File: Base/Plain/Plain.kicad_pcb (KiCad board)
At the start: 2 copper layers, 30 x 84 mm, 13 parts, among them J1 Barrel_Jack_Switch, J2 AudioJack2_Ground, J3 AudioJack2_Ground, J4 Conn_01x04_Pin, Q1 40V

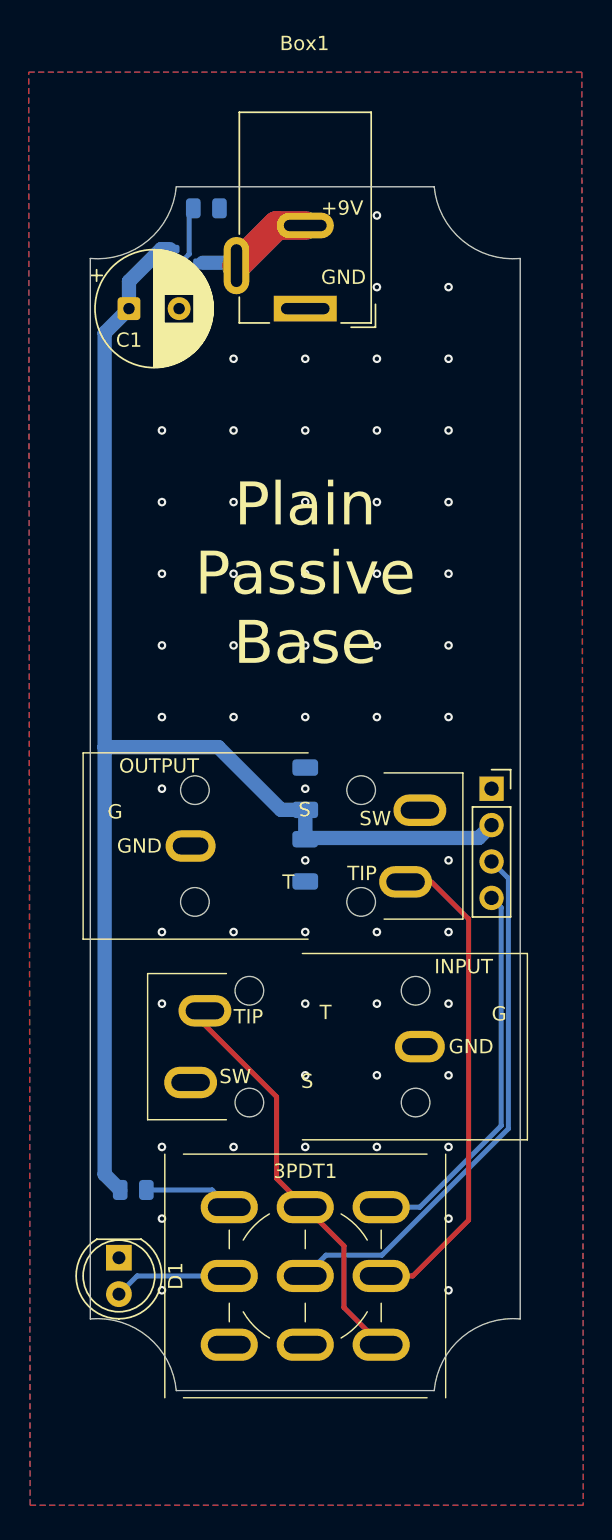
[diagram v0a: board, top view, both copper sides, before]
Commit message: First revisions from gen3 testing...
It turns out that while the single connector was sufficient, it is also
mechanically annoyingly less robust than the two separate pin headers we
used to have.

So even though we don't need the extra pins, just split it up into
"power" and a "signal" connectors again.  The placement behind the
output jack was good, so just put the power jack behind the input one
instead.

That ends up making routing nicer with the power trace going down where
it needs to be for the LED anyway, so it's a win-win.  Much nicer than
the old board.  And with the extra pins and the position right next to
the LED, lets just make the base board LED voltage available as an
"active" signal in case anybody ever wants it.

Also, just move the DC blocking capacitor and the anti-pop resistor to
ground to the base board.  Any effects board needs to do that, so it's
one less thing to worry about.  Also add back the low pass RF filter.

With the connector change, this obviously makes the new boards
incompatible, but it's not like I have any legacy boards except for the
test-boards.

On the effect board side, this does the layout changes, but also fixes
the Octaver board that was half-arsed and hadn't done proper bias
voltage calculations.  This basically just reuses them from the boost
board.

Plus use a JFET input on for the Octaver, and while at it make it also
just split the phase the natural way.  Both simpler and more balanced.

So maybe the Octaver works now.

And by "works", I obviously don't mean "sounds good".

Signed-off-by: Linus Torvalds <torvalds@linux-foundation.org>
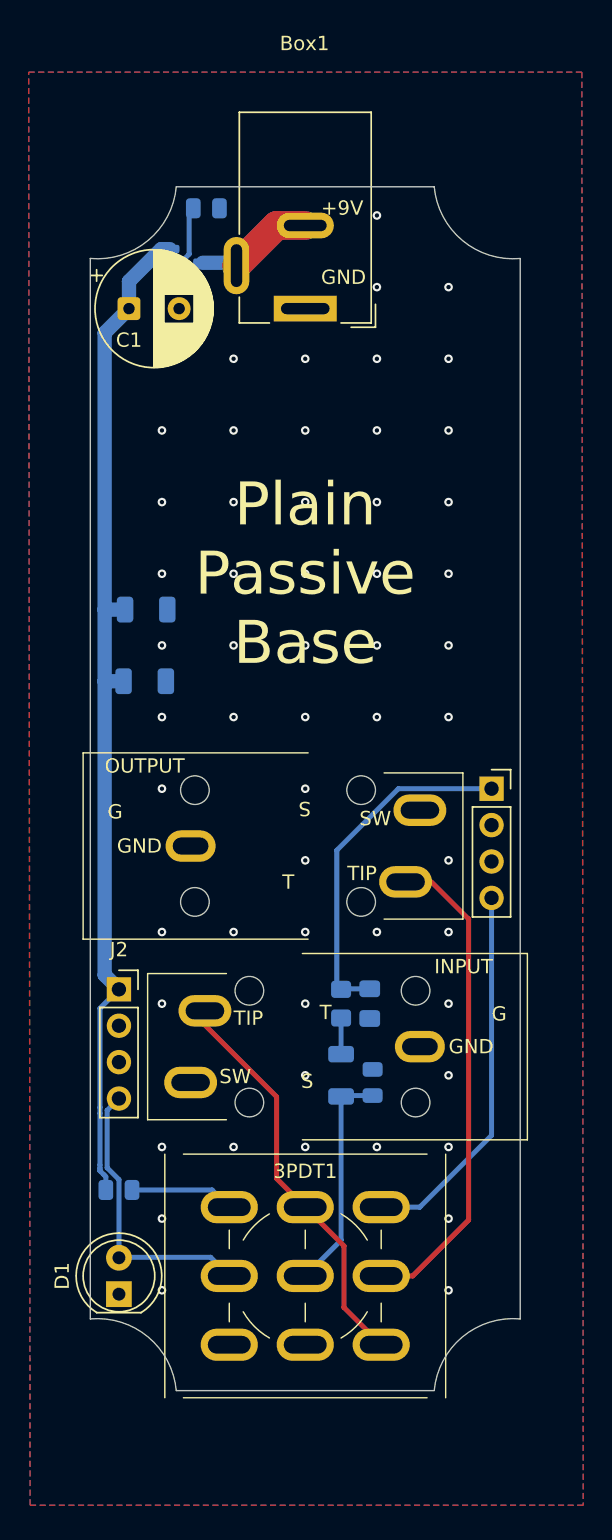
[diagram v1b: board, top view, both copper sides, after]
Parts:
- added C4: 0.47uF, Capacitor_SMD:C_1206_3216Metric, B.Cu at (102.5, 120.0)
- added C5: 220pF, Capacitor_SMD:C_0805_2012Metric_Pad1.18x1.45mm_HandSolder, B.Cu at (104.5, 115.0)
- added J2: Conn_01x04_Pin, Connector_PinSocket_2.54mm:PinSocket_1x04_P2.54mm_Vertical, F.Cu at (87.0, 114.0)
- added R3: 10k, Resistor_SMD:R_0805_2012Metric_Pad1.20x1.40mm_HandSolder, B.Cu at (102.5, 115.0)
- added R4: 1MEG, Resistor_SMD:R_0805_2012Metric, B.Cu at (104.7, 120.5)
- moved C3 16.8 mm to (88.8, 92.5), turned to 0 degrees
- moved C2 16.7 mm to (88.9, 87.5), turned to 0 degrees
- moved D1 2.54 mm to (87.0, 135.3), turned to 90 degrees
- moved R2 1.00 mm to (87.0, 128.0)
- renumbered J4 to J1, J2 to J3, J3 to J4, J1 to J5
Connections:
- net Net-(3PDT1A-A2) renamed LED
- 3PDT1 pad 5: IN^{EFF} -> Net-(3PDT1B-B2)
- J1 pad 1: GND -> IN^{EFF}
- J1 pad 2: VIN -> GND
- J1 pad 3: IN^{EFF} -> GND
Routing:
- net VIN: track 99.6 -> 71.8 mm
- net Net-(3PDT1B-B2): track 0.00 -> 15.8 mm
- net IN^{EFF}: track 37.6 -> 24.5 mm
- net LED: track 8.23 -> 20.0 mm
- net Net-(C4-Pad2): track 0.00 -> 2.53 mm
- net Net-(3PDT1A-A1): track 6.28 -> 7.28 mm
- net OUT^{EFF}: track 26.9 -> 26.3 mm
- net GND: vias 58 -> 56
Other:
- board text added: "R1: 100k (MOSFET gate) R2: 2k2 (LED) R3: 1k (RF filter) R4: 1M (anti-pop) C1: 100uF THT C2: 10uF C3: 1uF C4: 0.47uF (DC blocking) C5: 220pF (RF filter) Q1: PMV250 40V P-MOSFET"
- board text removed: "R1: 100k R2: 2k2 (LED) C1: 100uF THT C2: 10uF C3: 1uF Q1: PMV250 40V P-MOSFET"

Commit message: added 3D missing models for Plain pcb
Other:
- board text added: "Barrel Jack 3D model designed from Wurth site: https://www.we-online.com/en/components/products/DC_POWER_JACKS_WR_DC"
